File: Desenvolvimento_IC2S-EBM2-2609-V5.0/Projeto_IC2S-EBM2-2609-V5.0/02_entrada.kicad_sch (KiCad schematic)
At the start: 15 parts

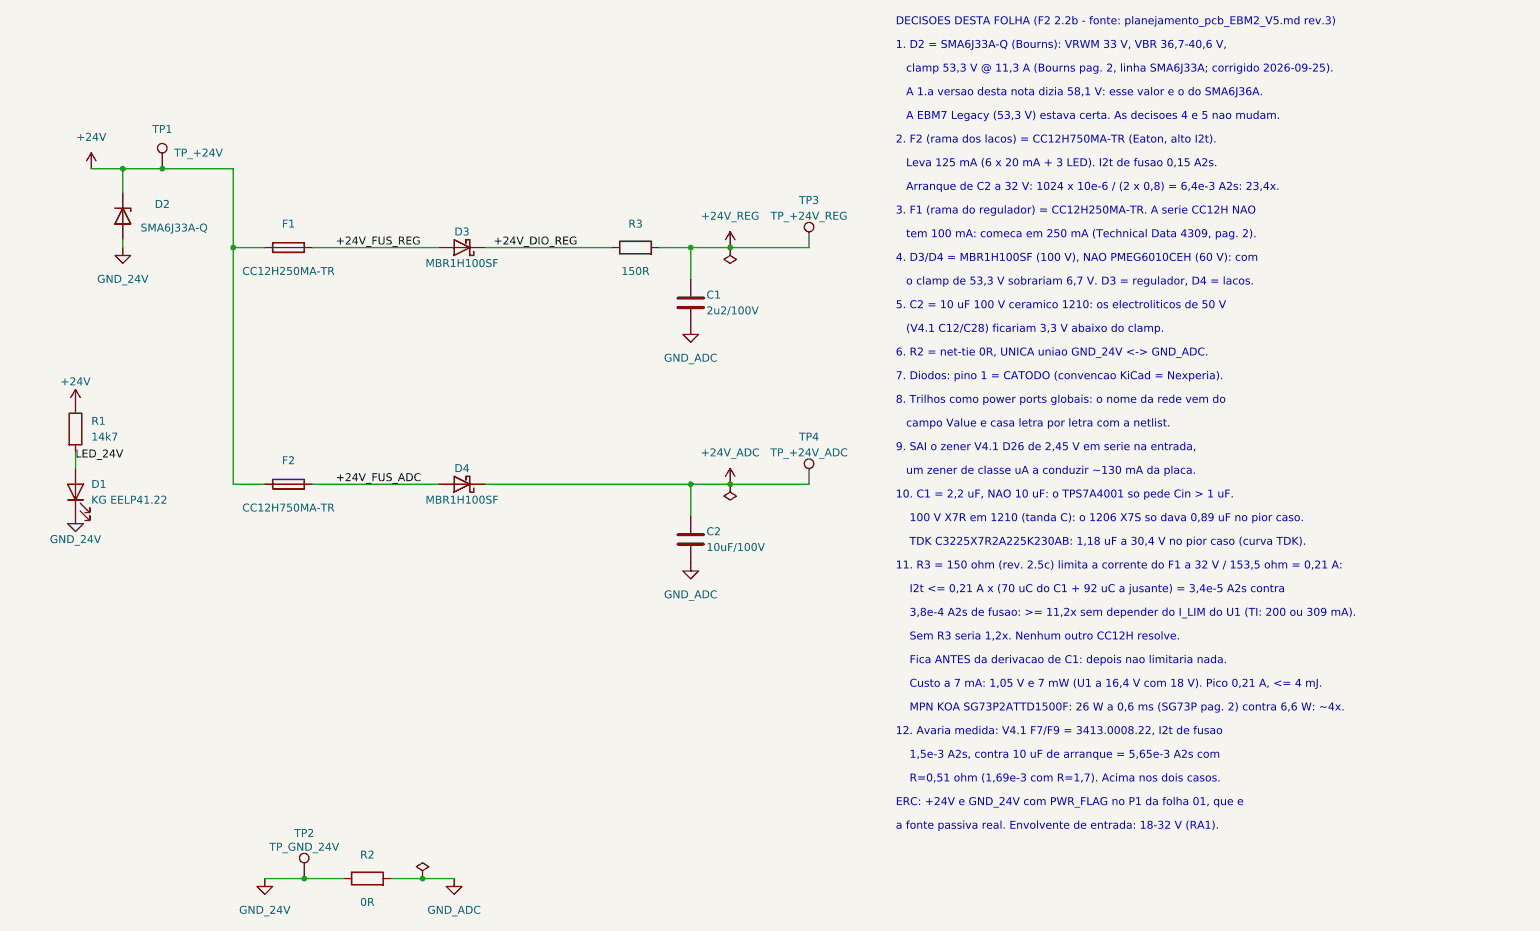
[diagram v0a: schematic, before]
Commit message: Revisao de 28-09 (vinda da EBM7): ramo unico de 24 V, 100 nF a 50 V, um so MPN de 1 uF
- Saem F1 (250 mA), D3 e R3: o F1 nao aguenta o arranque da placa toda e o R3
  so existia para o limitar. F2 + D4 alimentam o U1 e os lacos; +24V_REG passa
  a +24V_ADC. C1 fica (Cin do TPS7A4001). Esquematico e PCB (sem pistas).
- 100 nF fora do 24 V -> TDK C1608X7R1H104K080AA (50 V); C29 (+24V_ADC) fica
  GRM188R72A104KA35D (100 V). 1 uF -> TDK C1608X7R1H105K080AB.
- Folha 2 notas 3, 11, 13 e 14; BOM preliminar regenerada; README, registo e
  lista de datasheets. Alteracao posterior ao Portao 1, registada como tal.

Co-Authored-By: Claude Opus 5.5 (1M context) <noreply@anthropic.com>
Claude-Session: https://claude.ai/code/session_01KPnkiJQKrkjgRqqw9M78ie
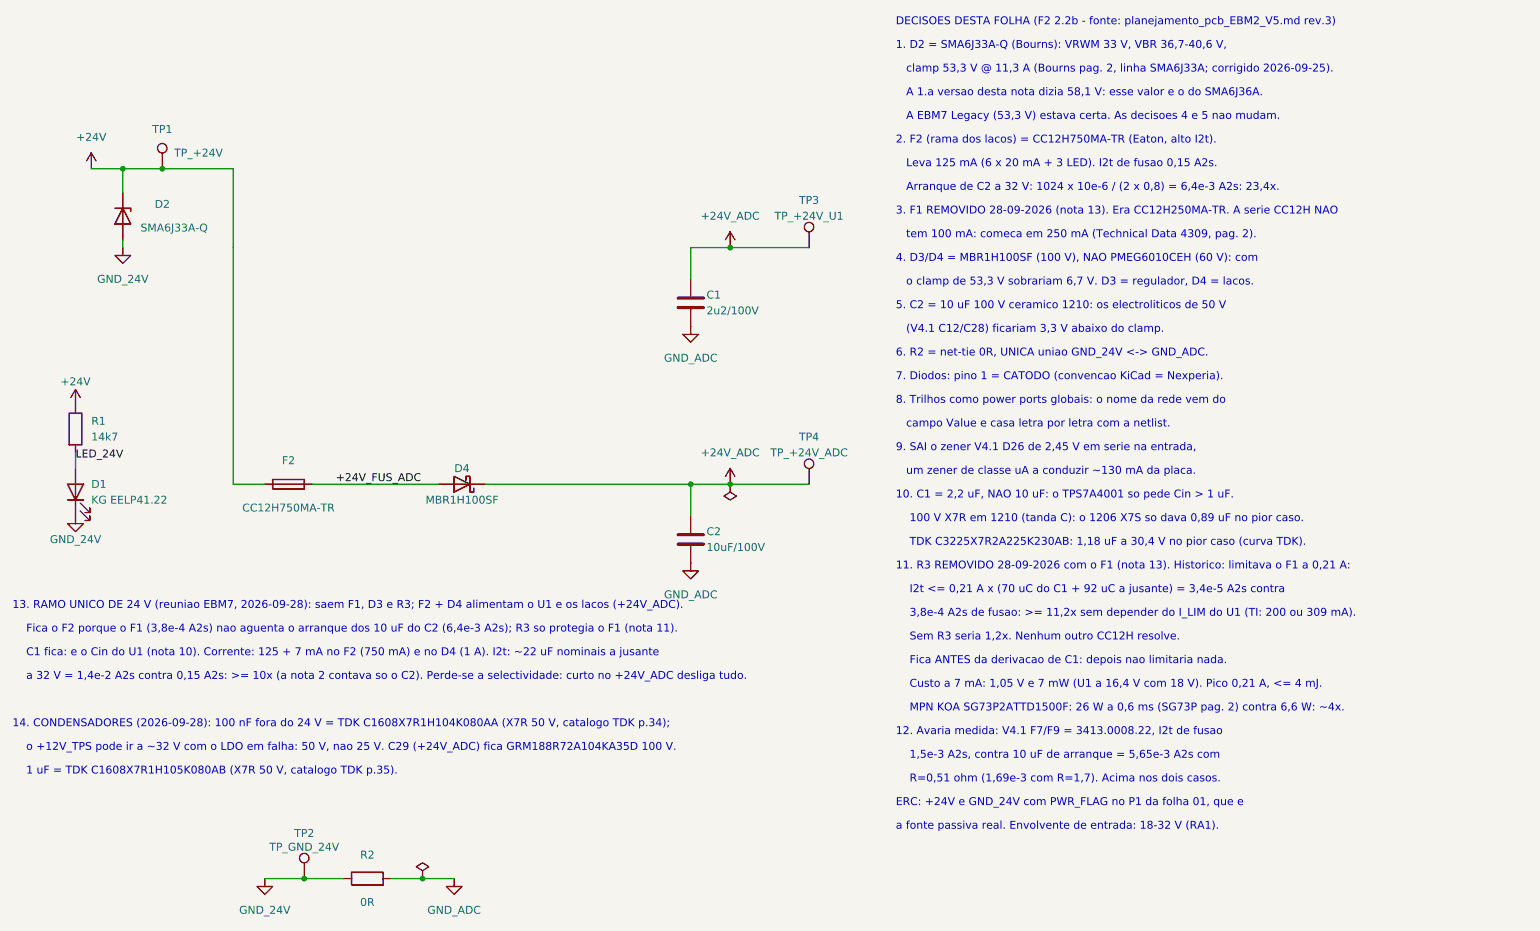
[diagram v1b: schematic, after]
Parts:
- removed D3: MBR1H100SF, EBM2_V5:SOD123, symbol Device:D_Schottky
- removed F1: CC12H250MA-TR, EBM2_V5:1206F, symbol Device:Fuse
- removed R3: 150R, EBM2_V5:0805R, symbol Device:R
- TP3: value TP_+24V_REG -> TP_+24V_U1
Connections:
- net +24V_REG is gone; now on net +24V_ADC: C1.1, TP3.1
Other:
- note added: "1 uF = TDK C1608X7R1H105K080AB (X7R 50 V, catalogo TDK p.35)."
- note added: "11. R3 REMOVIDO 28-09-2026 com o F1 (nota 13). Historico: limitava o F1 a 0,21 A:"
- note added: "13. RAMO UNICO DE 24 V (reuniao EBM7, 2026-09-28): saem F1, D3 e R3; F2 + D4 alimentam o U1 e os lacos (+24V_ADC)."
- note added: "14. CONDENSADORES (2026-09-28): 100 nF fora do 24 V = TDK C1608X7R1H104K080AA (X7R 50 V, catalogo TDK p.34);"
- note added: "3. F1 REMOVIDO 28-09-2026 (nota 13). Era CC12H250MA-TR. A serie CC12H NAO"
- note added: "C1 fica: e o Cin do U1 (nota 10). Corrente: 125 + 7 mA no F2 (750 mA) e no D4 (1 A). I2t: ~22 uF nominais a jusante"
- note added: "Fica o F2 porque o F1 (3,8e-4 A2s) nao aguenta o arranque dos 10 uF do C2 (6,4e-3 A2s); R3 so protegia o F1 (nota 11)."
- note added: "a 32 V = 1,4e-2 A2s contra 0,15 A2s: >= 10x (a nota 2 contava so o C2). Perde-se a selectividade: curto no +24V_ADC desliga tudo."
- note added: "o +12V_TPS pode ir a ~32 V com o LDO em falha: 50 V, nao 25 V. C29 (+24V_ADC) fica GRM188R72A104KA35D 100 V."
- note removed: "11. R3 = 150 ohm (rev. 2.5c) limita a corrente do F1 a 32 V / 153,5 ohm = 0,21 A:"
- note removed: "3. F1 (rama do regulador) = CC12H250MA-TR. A serie CC12H NAO"
